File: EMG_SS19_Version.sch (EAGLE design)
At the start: 219 parts, among them SW1 B3S-1000, SW2 B3S-1000, SW3 B3S-1000, SW4 B3S-1000, SW5 B3S-1000, T11 OPA388, T12 OPA388, T21 OPA388, T22 OPA388

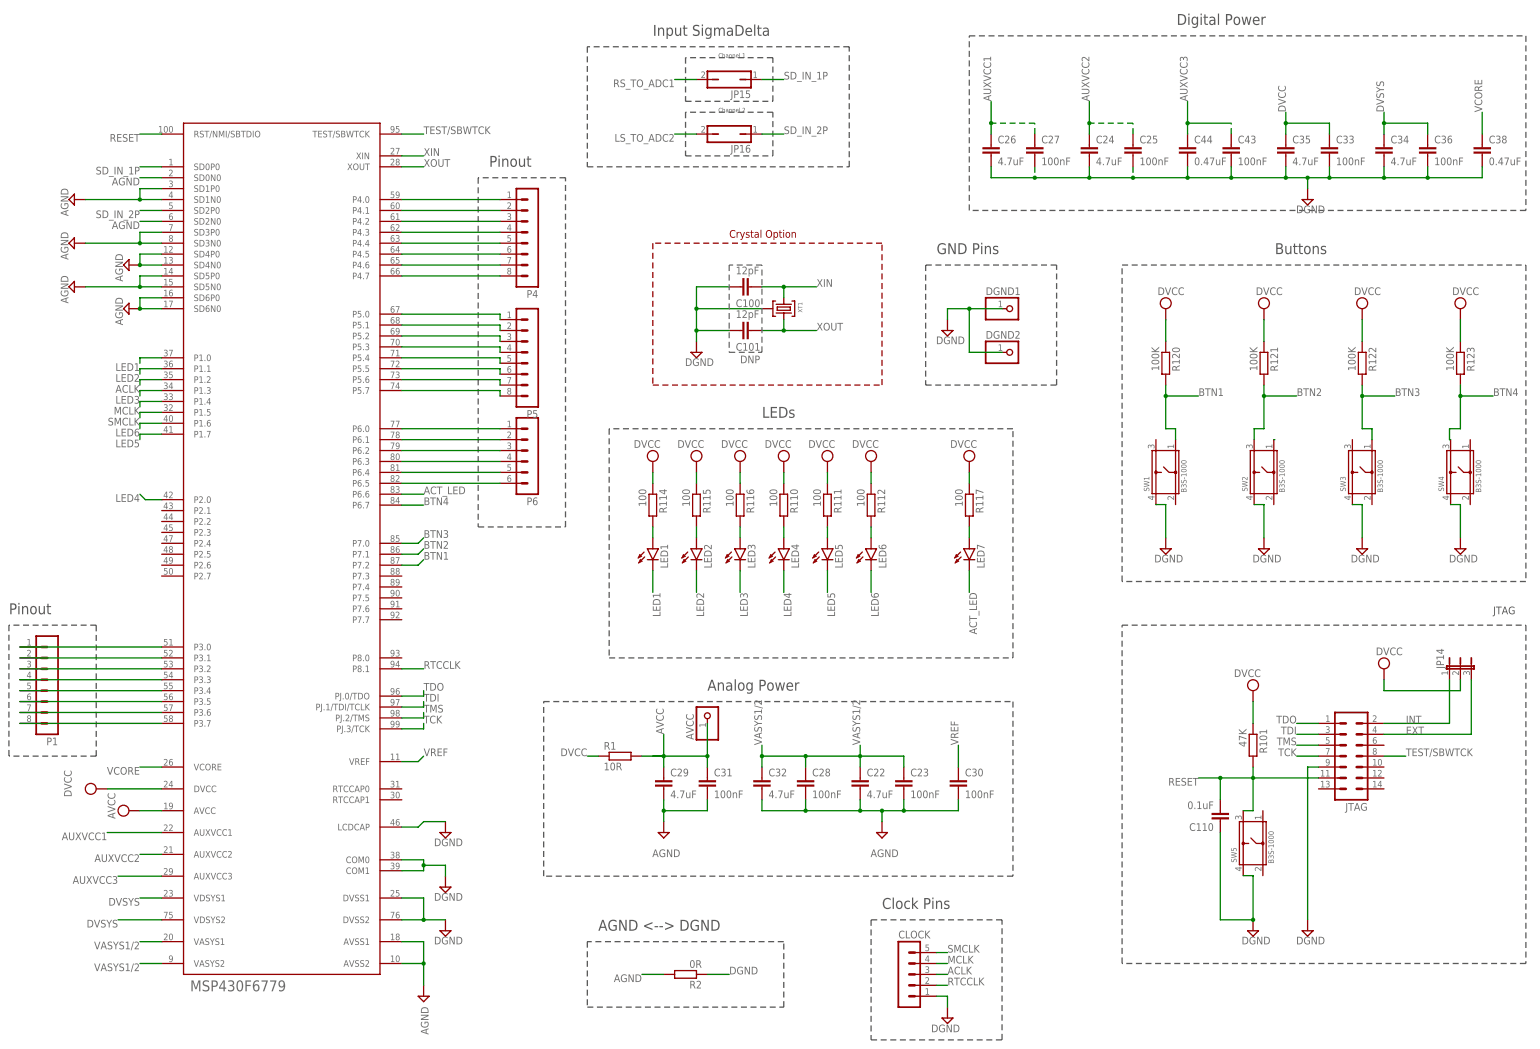
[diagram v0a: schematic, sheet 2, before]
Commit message: Fixed 3 buttons Added UART as back-channel to JTAG header acc. http://www.ti.com/lit/ug/slau647m/slau647m.pdf p.19
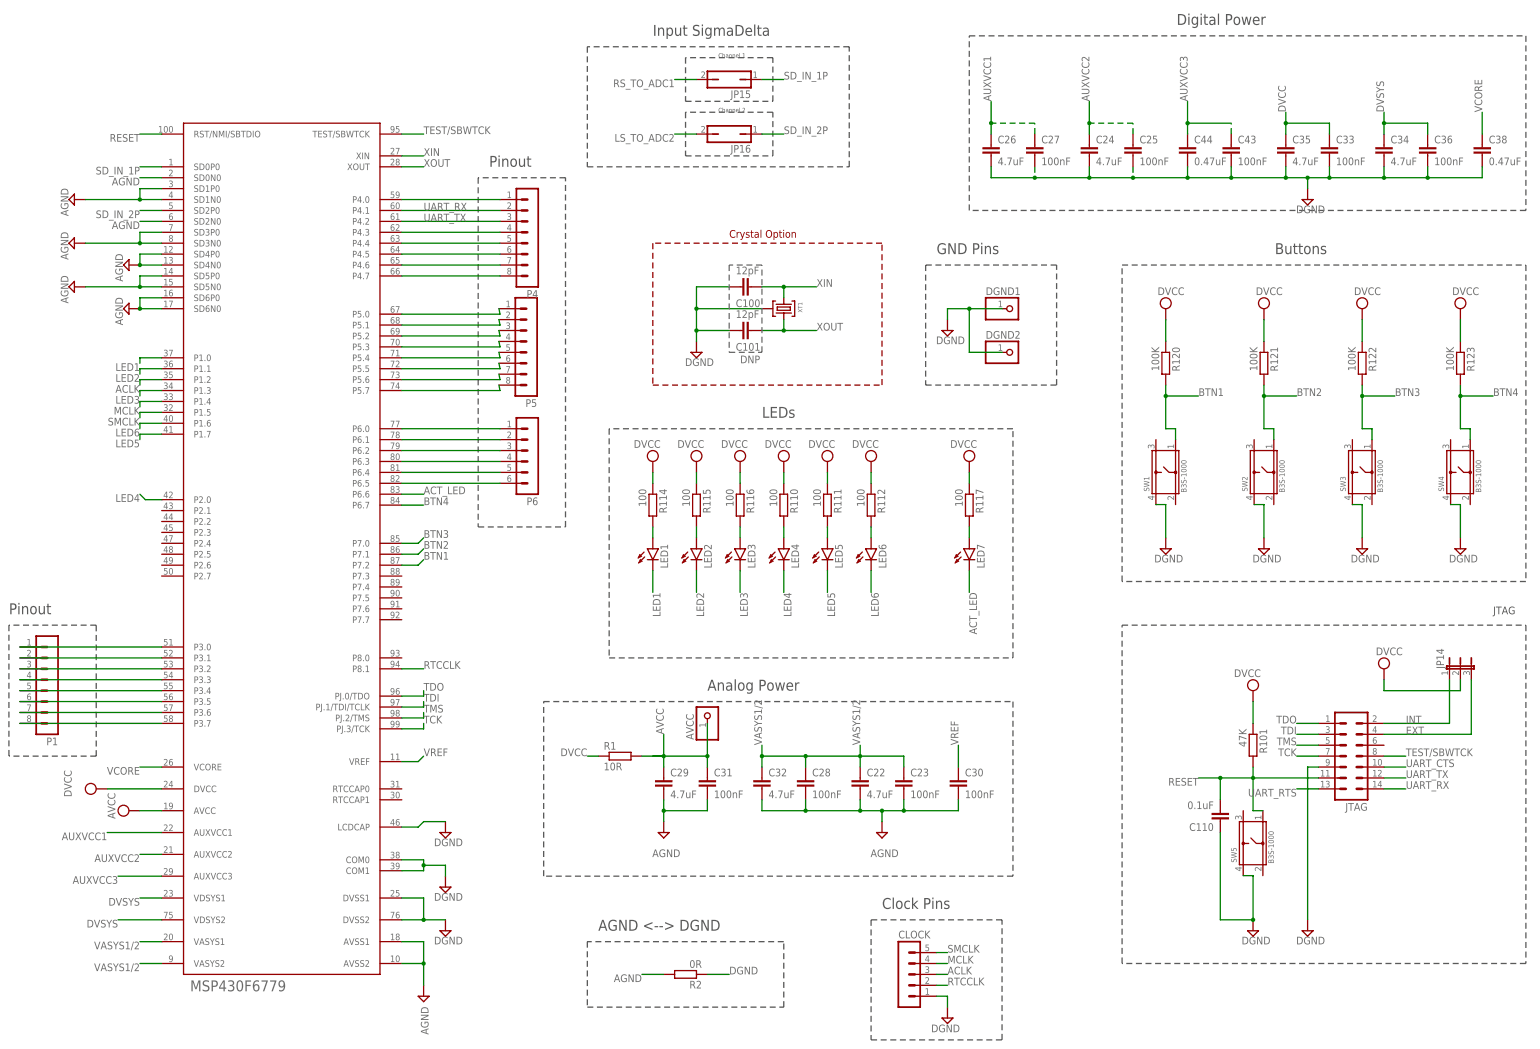
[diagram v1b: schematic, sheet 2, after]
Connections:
- removed net N$56: SW2.1
- removed net P4.1: P4.2, U$1.P4.1
- removed net P4.2: P4.3, U$1.P4.2
- new net UART_CTS: JTAG.10
- new net UART_RTS: JTAG.13
- new net UART_RX: JTAG.14, P4.2, U$1.P4.1
- new net UART_TX: JTAG.12, P4.3, U$1.P4.2
- net BTN2: now also SW2.1; no longer SW2.3
- net BTN4: now also SW4.1; no longer SW4.3
- net RESET: now also SW5.1; no longer SW5.3
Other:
- moved on the sheet: P5
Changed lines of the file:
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@@
 <?xml version="1.0" encoding="utf-8"?>
 <!DOCTYPE eagle SYSTEM "eagle.dtd">
-<eagle version="9.4.2">
+<eagle version="9.4.1">
 <drawing>
 <settings>
@@
 <attribute name="VALUE" x="156.21" y="75.438" size="1.778" layer="96"/>
 </instance>
-<instance part="P5" gate="1" x="139.7" y="172.72" smashed="yes" rot="R180">
-<attribute name="VALUE" x="140.97" y="185.42" size="1.778" layer="96" rot="R180"/>
-<attribute name="NAME" x="140.97" y="159.258" size="1.778" layer="95" rot="R180"/>
+<instance part="P5" gate="1" x="139.446" y="175.26" smashed="yes" rot="R180">
+<attribute name="VALUE" x="140.716" y="187.96" size="1.778" layer="96" rot="R180"/>
+<attribute name="NAME" x="140.716" y="161.798" size="1.778" layer="95" rot="R180"/>
 </instance>
 <instance part="P4" gate="1" x="139.7" y="200.66" smashed="yes" rot="R180">
@@
 <pinref part="JTAG" gate="1" pin="11"/>
 <wire x1="307.34" y1="73.66" x2="307.34" y2="66.04" width="0.1524" layer="91"/>
-<pinref part="SW5" gate="G$1" pin="3"/>
-<wire x1="305.054" y1="66.04" x2="307.34" y2="66.04" width="0.1524" layer="91"/>
+<pinref part="SW5" gate="G$1" pin="1"/>
+<wire x1="307.34" y1="66.04" x2="309.626" y2="66.04" width="0.1524" layer="91"/>
 </segment>
 <segment>
@@
 <pinref part="R121" gate="G$1" pin="2"/>
 <wire x1="309.88" y1="162.56" x2="309.88" y2="154.94" width="0.1524" layer="91"/>
-<pinref part="SW2" gate="G$1" pin="3"/>
-<wire x1="307.594" y1="152.4" x2="307.594" y2="154.94" width="0.1524" layer="91"/>
-<wire x1="307.594" y1="154.94" x2="309.88" y2="154.94" width="0.1524" layer="91"/>
+<pinref part="SW2" gate="G$1" pin="1"/>
+<wire x1="309.88" y1="154.94" x2="312.166" y2="154.94" width="0.1524" layer="91"/>
+<wire x1="312.166" y1="154.94" x2="312.166" y2="152.4" width="0.1524" layer="91"/>
 </segment>
 <segment>
@@
 <pinref part="R123" gate="G$1" pin="2"/>
 <wire x1="355.6" y1="154.94" x2="355.6" y2="162.56" width="0.1524" layer="91"/>
-<wire x1="355.6" y1="154.94" x2="353.06" y2="154.94" width="0.1524" layer="91"/>
-<pinref part="SW4" gate="G$1" pin="3"/>
-<wire x1="353.06" y1="154.94" x2="353.06" y2="152.4" width="0.1524" layer="91"/>
-<wire x1="353.06" y1="152.4" x2="353.314" y2="152.4" width="0.1524" layer="91"/>
+<pinref part="SW4" gate="G$1" pin="1"/>
+<wire x1="355.6" y1="154.94" x2="357.886" y2="154.94" width="0.1524" layer="91"/>
+<wire x1="357.886" y1="154.94" x2="357.886" y2="152.4" width="0.1524" layer="91"/>
 </segment>
 <segment>
@@
 </segment>
 </net>
-<net name="P4.1" class="0">
-<segment>
-<pinref part="U$1" gate="G$1" pin="P4.1"/>
-<pinref part="P4" gate="1" pin="2"/>
-<wire x1="109.22" y1="205.74" x2="132.08" y2="205.74" width="0.1524" layer="91"/>
-</segment>
-</net>
-<net name="P4.2" class="0">
-<segment>
-<pinref part="U$1" gate="G$1" pin="P4.2"/>
-<pinref part="P4" gate="1" pin="3"/>
-<wire x1="109.22" y1="203.2" x2="132.08" y2="203.2" width="0.1524" layer="91"/>
-</segment>
-</net>
 <net name="P4.3" class="0">
 <segment>
@@
 <pinref part="P5" gate="1" pin="1"/>
 <wire x1="109.22" y1="181.61" x2="132.08" y2="181.61" width="0.1524" layer="91"/>
-<wire x1="132.08" y1="181.61" x2="132.08" y2="180.34" width="0.1524" layer="91"/>
+<wire x1="132.08" y1="181.61" x2="131.826" y2="182.88" width="0.1524" layer="91"/>
 </segment>
 </net>
@@
 <pinref part="P5" gate="1" pin="2"/>
 <wire x1="109.22" y1="179.07" x2="132.08" y2="179.07" width="0.1524" layer="91"/>
-<wire x1="132.08" y1="179.07" x2="132.08" y2="177.8" width="0.1524" layer="91"/>
+<wire x1="132.08" y1="179.07" x2="131.826" y2="180.34" width="0.1524" layer="91"/>
 </segment>
 </net>
@@
 <pinref part="P5" gate="1" pin="3"/>
 <wire x1="109.22" y1="176.53" x2="132.08" y2="176.53" width="0.1524" layer="91"/>
-<wire x1="132.08" y1="176.53" x2="132.08" y2="175.26" width="0.1524" layer="91"/>
+<wire x1="132.08" y1="176.53" x2="131.826" y2="177.8" width="0.1524" layer="91"/>
 </segment>
 </net>
@@
 <pinref part="P5" gate="1" pin="4"/>
 <wire x1="109.22" y1="173.99" x2="132.08" y2="173.99" width="0.1524" layer="91"/>
-<wire x1="132.08" y1="173.99" x2="132.08" y2="172.72" width="0.1524" layer="91"/>
+<wire x1="132.08" y1="173.99" x2="131.826" y2="175.26" width="0.1524" layer="91"/>
 </segment>
 </net>
@@
 <pinref part="P5" gate="1" pin="5"/>
 <wire x1="109.22" y1="171.45" x2="132.08" y2="171.45" width="0.1524" layer="91"/>
-<wire x1="132.08" y1="171.45" x2="132.08" y2="170.18" width="0.1524" layer="91"/>
+<wire x1="132.08" y1="171.45" x2="131.826" y2="172.72" width="0.1524" layer="91"/>
 </segment>
 </net>
@@
 <pinref part="P5" gate="1" pin="6"/>
 <wire x1="109.22" y1="168.91" x2="132.08" y2="168.91" width="0.1524" layer="91"/>
-<wire x1="132.08" y1="168.91" x2="132.08" y2="167.64" width="0.1524" layer="91"/>
+<wire x1="132.08" y1="168.91" x2="131.826" y2="170.18" width="0.1524" layer="91"/>
 </segment>
 </net>
@@
 <pinref part="P5" gate="1" pin="7"/>
 <wire x1="109.22" y1="166.37" x2="132.08" y2="166.37" width="0.1524" layer="91"/>
-<wire x1="132.08" y1="166.37" x2="132.08" y2="165.1" width="0.1524" layer="91"/>
+<wire x1="132.08" y1="166.37" x2="131.826" y2="167.64" width="0.1524" layer="91"/>
 </segment>
 </net>
@@
 <pinref part="P5" gate="1" pin="8"/>
 <wire x1="109.22" y1="163.83" x2="132.08" y2="163.83" width="0.1524" layer="91"/>
-<wire x1="132.08" y1="163.83" x2="132.08" y2="162.56" width="0.1524" layer="91"/>
+<wire x1="132.08" y1="163.83" x2="131.826" y2="165.1" width="0.1524" layer="91"/>
 </segment>
 </net>
@@
 </segment>
 </net>
-<net name="N$56" class="0">
+<net name="UART_CTS" class="0">
 <segment>
-<pinref part="SW2" gate="G$1" pin="1"/>
-<wire x1="312.42" y1="152.4" x2="312.166" y2="152.4" width="0.1524" layer="91"/>
+<pinref part="JTAG" gate="1" pin="10"/>
+<wire x1="337.82" y1="76.2" x2="342.9" y2="76.2" width="0.1524" layer="91"/>
+<label x="342.9" y="76.2" size="1.778" layer="95"/>
+</segment>
+</net>
+<net name="UART_TX" class="0">
+<segment>
+<pinref part="JTAG" gate="1" pin="12"/>
+<wire x1="337.82" y1="73.66" x2="342.9" y2="73.66" width="0.1524" layer="91"/>
+<label x="342.9" y="73.66" size="1.778" layer="95"/>
+</segment>
+<segment>
+<pinref part="U$1" gate="G$1" pin="P4.2"/>
+<pinref part="P4" gate="1" pin="3"/>
+<wire x1="109.22" y1="203.2" x2="132.08" y2="203.2" width="0.1524" layer="91"/>
+<label x="114.3" y="203.2" size="1.778" layer="95"/>
+</segment>
+</net>
+<net name="UART_RX" class="0">
+<segment>
+<pinref part="JTAG" gate="1" pin="14"/>
+<wire x1="337.82" y1="71.12" x2="342.9" y2="71.12" width="0.1524" layer="91"/>
+<label x="342.9" y="71.12" size="1.778" layer="95"/>
+</segment>
+<segment>
+<pinref part="U$1" gate="G$1" pin="P4.1"/>
+<pinref part="P4" gate="1" pin="2"/>
+<wire x1="109.22" y1="205.74" x2="132.08" y2="205.74" width="0.1524" layer="91"/>
+<label x="114.3" y="205.74" size="1.778" layer="95"/>
+</segment>
+</net>
+<net name="UART_RTS" class="0">
+<segment>
+<pinref part="JTAG" gate="1" pin="13"/>
+<wire x1="322.58" y1="71.12" x2="317.5" y2="71.12" width="0.1524" layer="91"/>
+<label x="317.5" y="71.12" size="1.778" layer="95" rot="R180"/>
 </segment>
 </net>
